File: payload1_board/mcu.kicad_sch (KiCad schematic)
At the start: 8 parts, among them U1 ATSAMD21G18A-AF

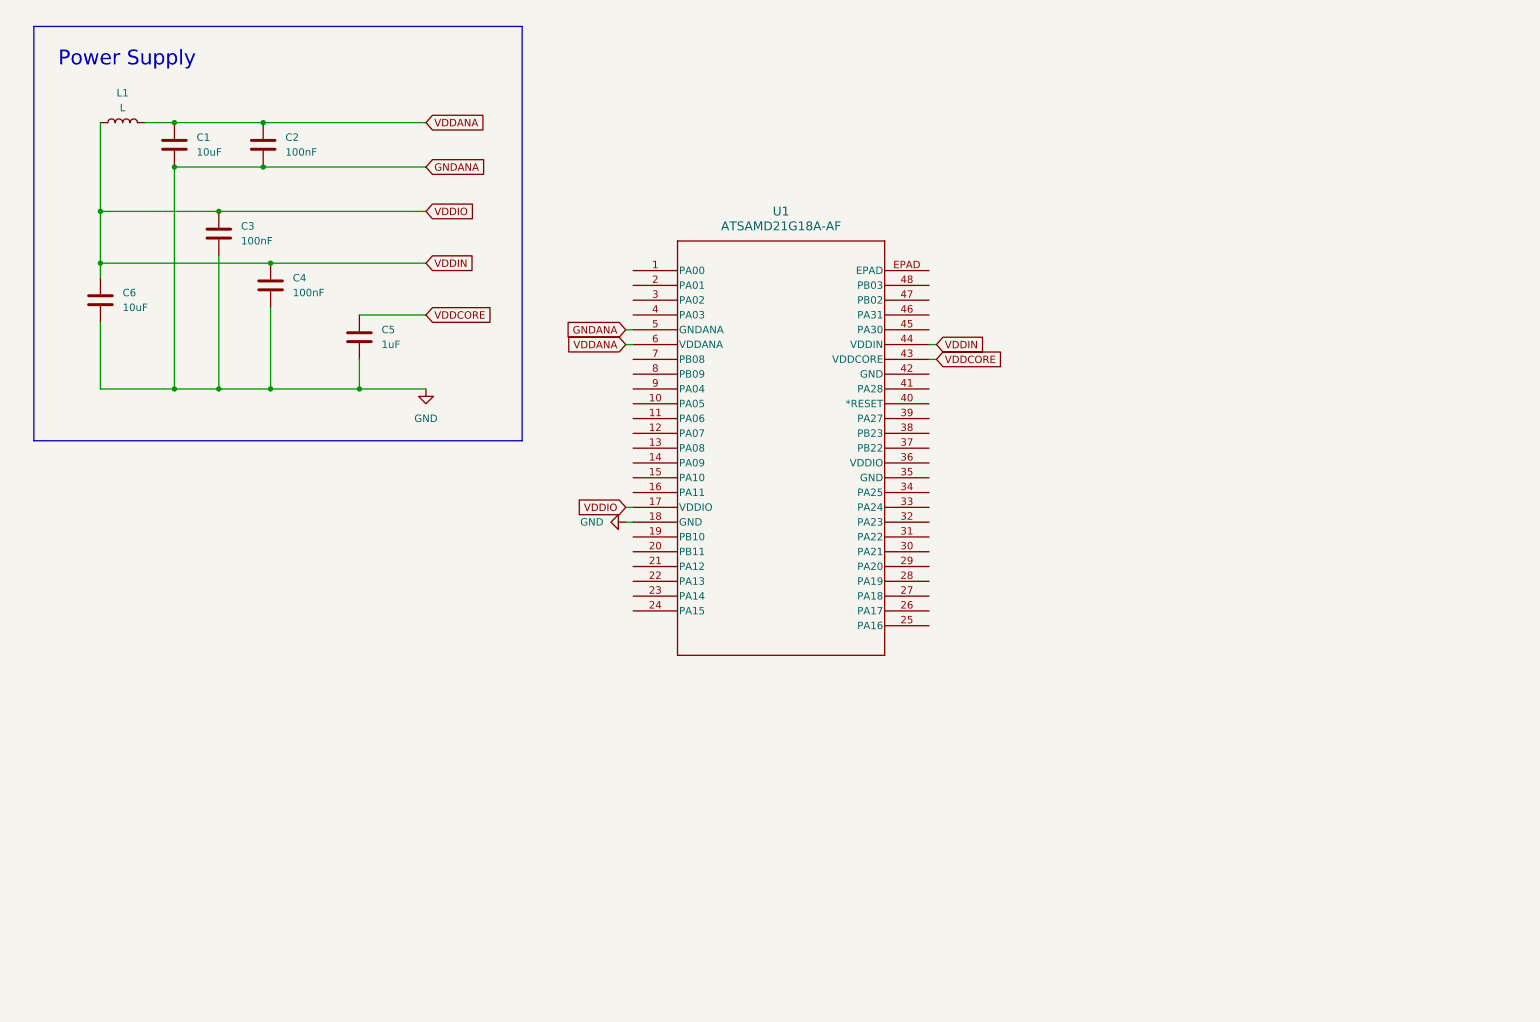
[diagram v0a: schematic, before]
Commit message: Power circuit for SAMD21
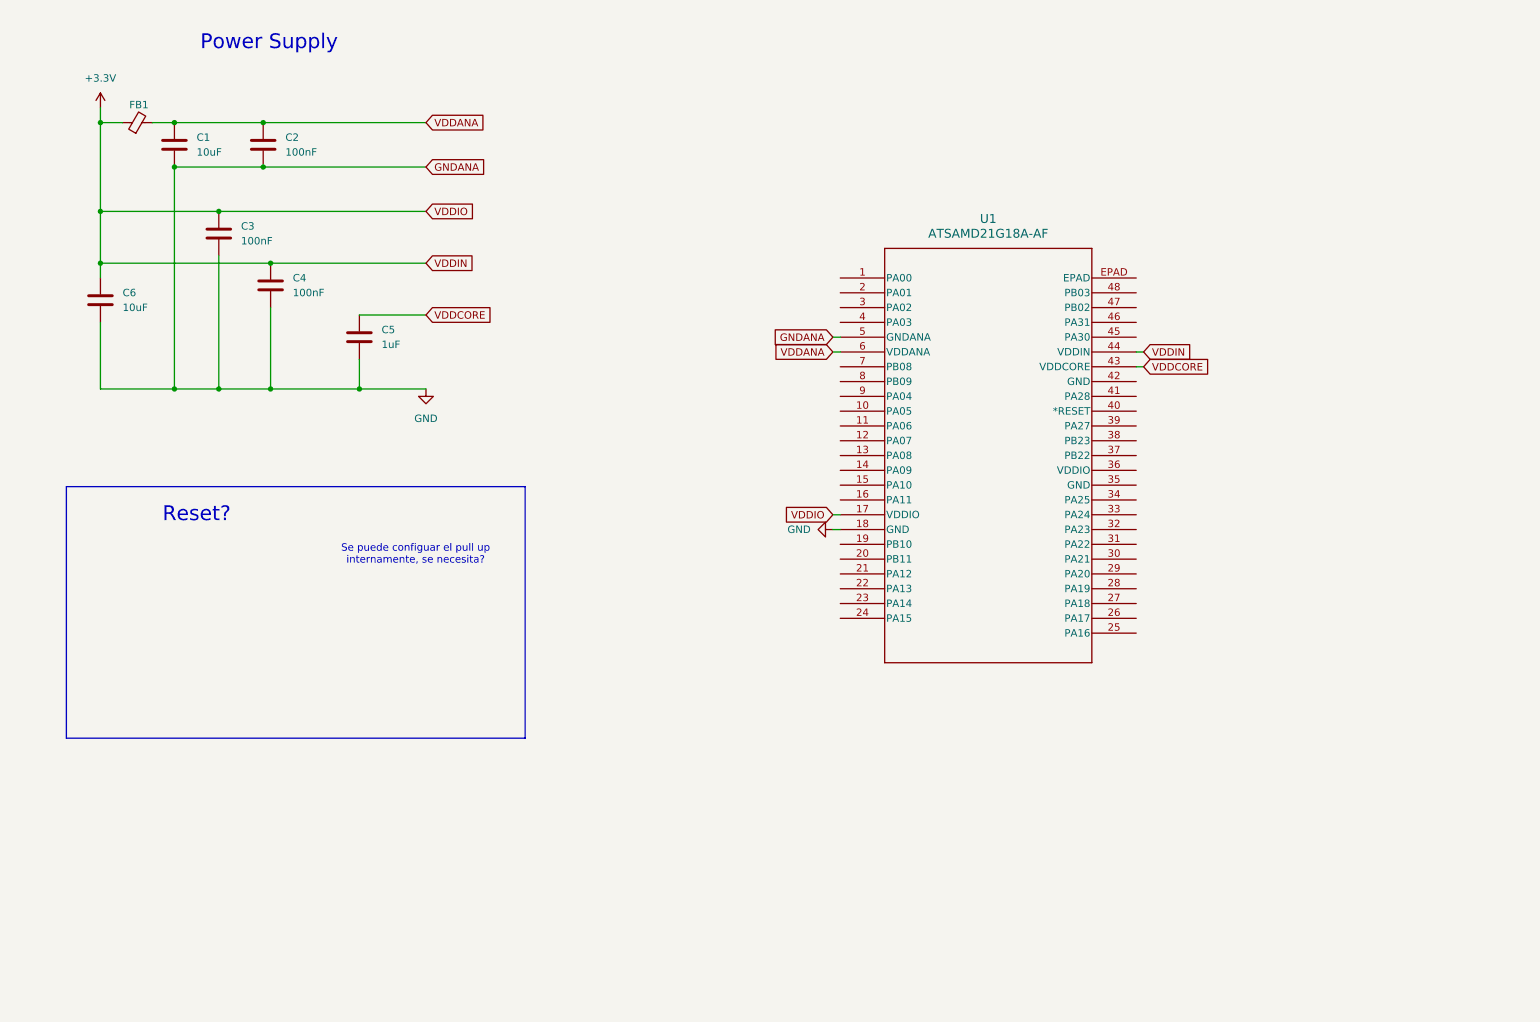
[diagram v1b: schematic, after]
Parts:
- removed L1: L, symbol Device:L
- added FB1: FerriteBead_Small, symbol Device:FerriteBead_Small
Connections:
- net VDDANA: now also FB1.2
- net VDDIN renamed +3.3V
- net +3.3V: now also FB1.1
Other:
- note added: "Reset?"
- note added: "Se puede configuar el pull up internamente, se necesita?"
- moved on the sheet: U1

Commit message: update schematic libraries
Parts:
- U1: footprint TQFP48_7x7MC_MCH -> (none)
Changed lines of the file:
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@@
 			)
 		)
-		(property "Footprint" "TQFP48_7x7MC_MCH"
+		(property "Footprint" ""
 			(at 157.48 60.96 0)
 			(effects

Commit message: Update schematic
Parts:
- removed FB1: FerriteBead_Small, symbol Device:FerriteBead_Small
- removed U1: ATSAMD21G18A-AF, symbol SAMD21G18A-AF:ATSAMD21G18A-AF
- added C10, C37: 4.7uF, symbol Device:C
- added C11, C12, C16, C7: 100nF, symbol Device:C
- added C14: 0.47uF, symbol Device:C
- added C26, C31, C8, C9: 6.8pF, symbol Device:C
- added C32, C33, C34: 33pF, symbol Device:C
- added D1: ESD, symbol Diode:ESD5Zxx
- added L1: 600R@100MHz, symbol Device:FerriteBead_Small
- added L2: 15uH, symbol Device:L
- added R1: 10K, symbol Device:R
- added SB1, SB11, SB13, SB14, SB2, SB7: Close, symbol Jumper:SolderJumper_2_Bridged
- added SB8: Open, symbol Jumper:SolderJumper_2_Open
- added U1: STM32WLE5CCU6, UFQFPN48_STM, symbol STM32WLE5:STM32WLE5CCU6
- added Y1: 32.768KHz, symbol Device:Crystal_GND24_Small
- added Y2: 32MHz, symbol Device:Crystal_GND24_Small
- C1: value 10uF -> 4.7uF
- C5: value 1uF -> 100nF
- C6: value 10uF -> 4.7nF
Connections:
- net VDDANA is gone; now on net GND: C1.1, C2.1
- net VDDCORE is gone; now on net GND: C5.1
- net GND: now also C3.1, C4.1, C10.2, C11.2, C12.2, C14.2, C16.2, C26.1, C31.1, C32.2, C33.2, C34.2, C37.2, C7.2, C8.1, C9.1, D1.2 (A), R1.2, U1.48 (VSSSMPS), U1.49 (GND), Y1.2 (G), Y1.4 (G), Y2.2 (G), Y2.4 (G); no longer C1.2, C2.2, C3.2, C4.2, C5.2
- removed net +3.3V: C3.1, C4.1, C6.1
- new net: C26.2, SB13.1 (A), Y2.1
- new net: C9.2, SB2.1 (A), Y1.3
- new net: C31.2, SB14.1 (A), Y2.3
- new net: C8.2, SB1.1 (A), Y1.1
- new net: R1.1, SB11.2 (B)
- new net NRST: C12.1, D1.1 (K), U1.18 (NRST)
- new net OSC_IN: SB13.2 (B), U1.26 (OSC_IN)
- new net OSC_OUT: SB14.2 (B), U1.27 (OSC_OUT)
- new net PA13: U1.36 (PA13)
- new net PB0: U1.30 (PB0-VDD_TCXO)
- new net PC13: U1.38 (PC13)
- new net PC14-OSC32_IN: SB1.2 (B), U1.39 (PC14-OSC32_IN)
- new net PC15-OSC32_OUT: SB2.2 (B), U1.40 (PC15-OSC32_OUT)
- new net PH3: SB11.1 (A), U1.19 (PH3-BOOT0)
- new net RFI_N: U1.21 (RFI_N)
- new net RFI_P: U1.20 (RFI_P)
- new net RFO_HP: U1.23 (RFO_HP)
- new net VBAT: C1.2, C2.2, C3.2, C37.1, C4.2, C5.2, L1.2, U1.11 (VDD), U1.37 (VBAT), U1.44 (VDD)
- new net VDDA: C6.1, C7.1, L1.1, U1.41 (VDDA)
- new net VDDPA: C33.1, SB7.2 (B), SB8.1 (A), U1.25 (VDDPA)
- new net VDDRF: C10.1, C11.1, C32.1, SB7.1 (A), U1.28 (VDDRF), U1.46 (VDDSMPS)
- new net VDDRF1V55: C14.1, C16.1, C34.1, L2.2, SB8.2 (B), U1.29 (VDDRF1V55), U1.45 (VFBSMPS)
- new net VLXSMPS: L2.1, U1.47 (VLXSMPS)
- new net VR_PA: U1.24 (VR_PA)
- no-connect marks 0 -> 1
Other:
- note removed: "Power Supply"
- note removed: "Reset?"
- note removed: "Se puede configuar el pull up internamente, se necesita?"
